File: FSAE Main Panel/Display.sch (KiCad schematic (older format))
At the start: 7 parts

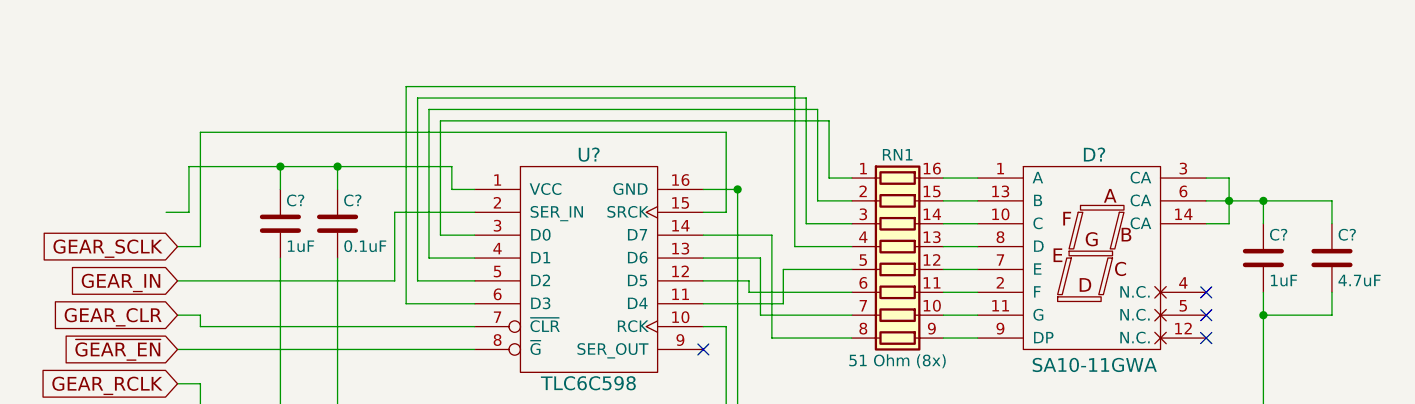
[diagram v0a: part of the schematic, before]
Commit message: Attempt to fix custom library pathing
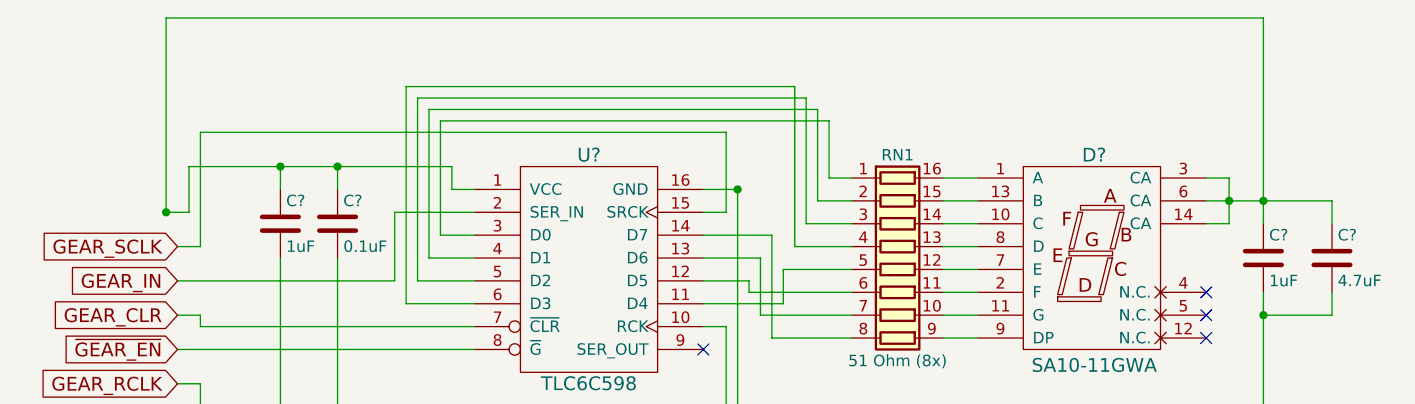
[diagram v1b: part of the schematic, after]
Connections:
- net at C?.1, C?.1, U?.1 (VCC): now also C?.1, C?.1, D?.14 (CA), D?.3 (CA), D?.6 (CA)
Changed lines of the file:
@@
 LIBS:contrib
 LIBS:valves
-LIBS:KingBright_Addition
-LIBS:TI_Additions
+LIBS:apa102c
+LIBS:lm2734
+LIBS:prtr5v0u2x
+LIBS:samd21g18a-au
 LIBS:FSAE Main Panel-cache
 EELAYER 25 0
@@
 $EndComp
 Wire Wire Line
-	6150 4900 6150 5000
+	6150 4100 6150 5000
 Wire Wire Line
 	6450 4900 6450 5000
@@
 	2100 5150 2100 5950
 Connection ~ 2100 5950
+Wire Wire Line
+	6150 4100 1350 4100
+Wire Wire Line
+	1350 4100 1350 4950
+Connection ~ 1350 4950
 $EndSCHEMATC

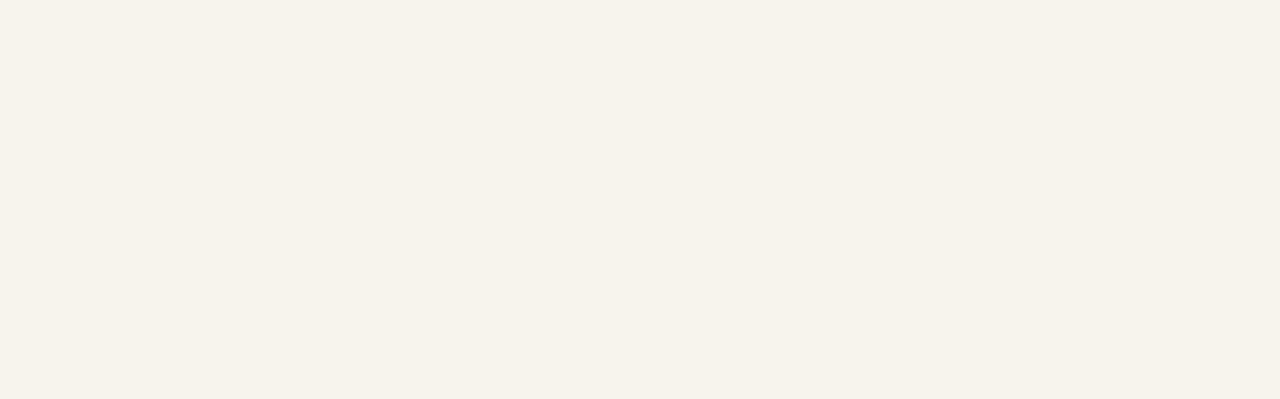
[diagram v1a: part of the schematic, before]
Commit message: Initial PCB layout
Started PCB layout with major dimensions.
Added RPM LEDs.
Rearranged the file structure for the librarys and the search paths.
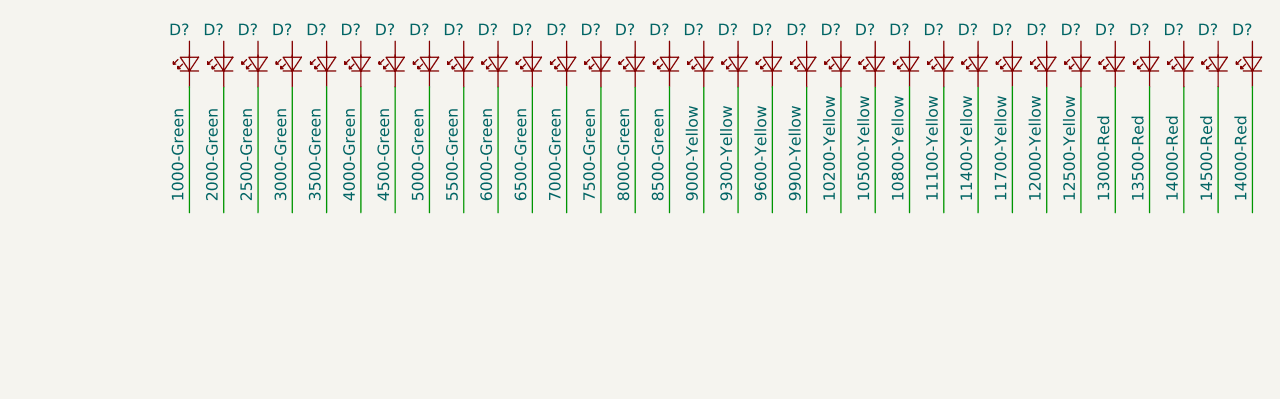
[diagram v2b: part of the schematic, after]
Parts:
- added D?: 2000-Green, OSRAM:D_0805, symbol LED_Small
- added D?: 1000-Green, OSRAM:D_0805, symbol LED_Small
- added D?: 2500-Green, OSRAM:D_0805, symbol LED_Small
- added D?: 3500-Green, OSRAM:D_0805, symbol LED_Small
- added D?: 3000-Green, OSRAM:D_0805, symbol LED_Small
- added D?: 4000-Green, OSRAM:D_0805, symbol LED_Small
- added D?: 5000-Green, OSRAM:D_0805, symbol LED_Small
- added D?: 4500-Green, OSRAM:D_0805, symbol LED_Small
- added D?: 5500-Green, OSRAM:D_0805, symbol LED_Small
- added D?: 6500-Green, OSRAM:D_0805, symbol LED_Small
- added D?: 6000-Green, OSRAM:D_0805, symbol LED_Small
- added D?: 7000-Green, OSRAM:D_0805, symbol LED_Small
- added D?: 8000-Green, OSRAM:D_0805, symbol LED_Small
- added D?: 7500-Green, OSRAM:D_0805, symbol LED_Small
- added D?: 8500-Green, OSRAM:D_0805, symbol LED_Small
- added D?: 9300-Yellow, OSRAM:D_0805, symbol LED_Small
- added D?: 9000-Yellow, OSRAM:D_0805, symbol LED_Small
- added D?: 9600-Yellow, OSRAM:D_0805, symbol LED_Small
- added D?: 10200-Yellow, OSRAM:D_0805, symbol LED_Small
- added D?: 9900-Yellow, OSRAM:D_0805, symbol LED_Small
- added D?: 10500-Yellow, OSRAM:D_0805, symbol LED_Small
- added D?: 11100-Yellow, OSRAM:D_0805, symbol LED_Small
- added D?: 10800-Yellow, OSRAM:D_0805, symbol LED_Small
- added D?: 11400-Yellow, OSRAM:D_0805, symbol LED_Small
- added D?: 11700-Yellow, OSRAM:D_0805, symbol LED_Small
- added D?: 12000-Yellow, OSRAM:D_0805, symbol LED_Small
- added D?: 13000-Red, OSRAM:D_0805, symbol LED_Small
- added D?: 12500-Yellow, OSRAM:D_0805, symbol LED_Small
- added D?: 13500-Red, OSRAM:D_0805, symbol LED_Small
- added D?: 14500-Red, OSRAM:D_0805, symbol LED_Small
- added D? (x2): 14000-Red, OSRAM:D_0805, symbol LED_Small
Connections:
- wire segments 80 -> 112

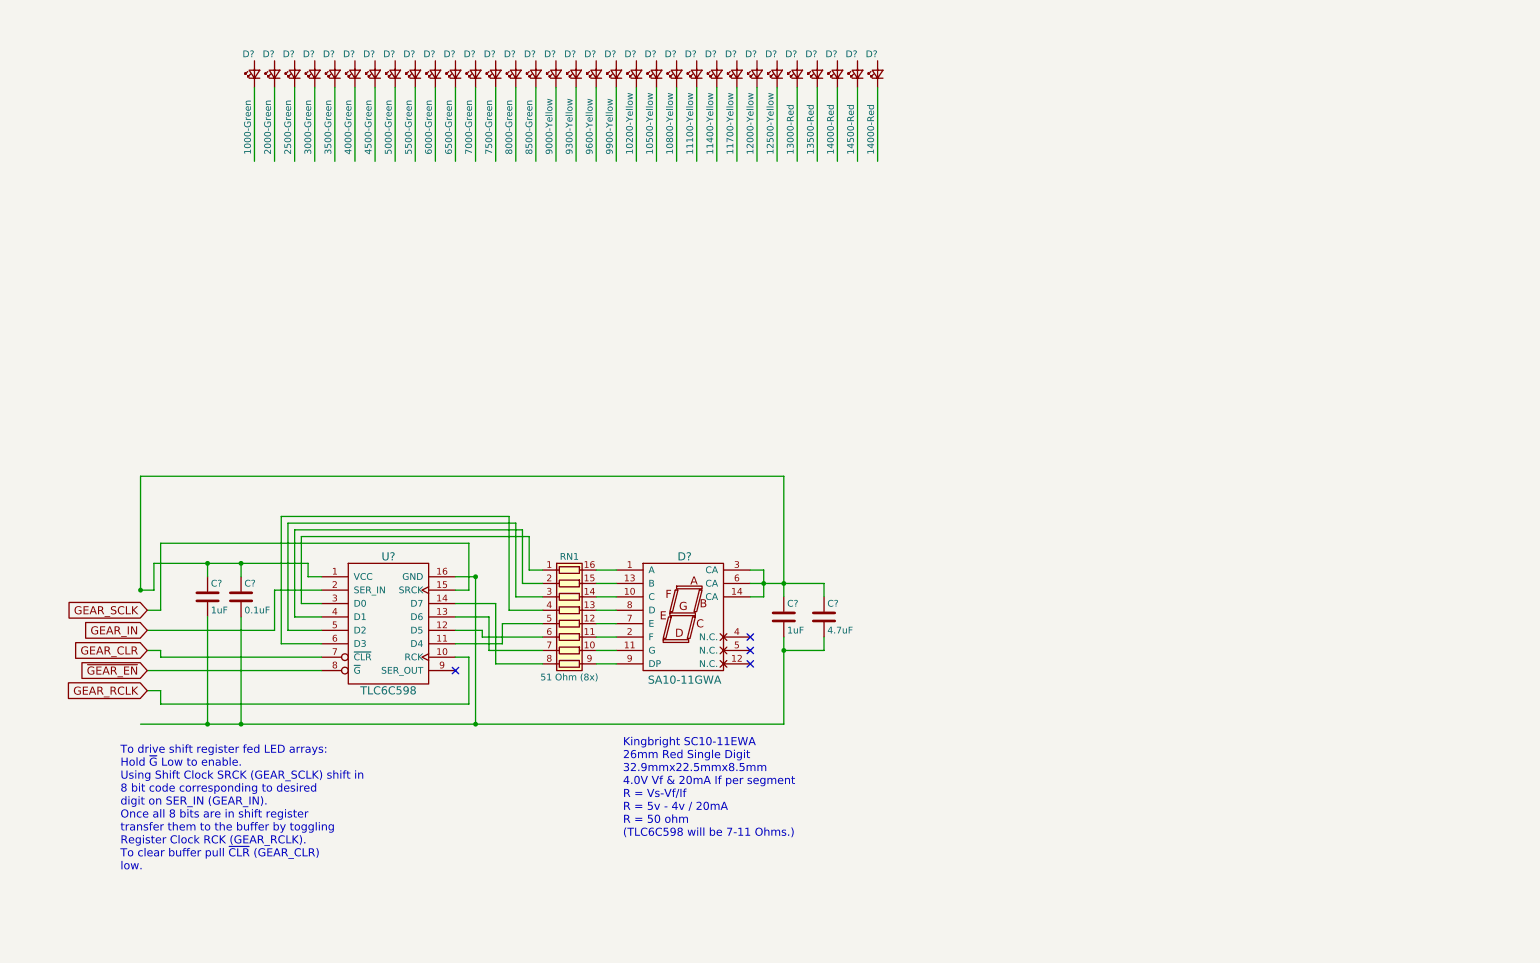
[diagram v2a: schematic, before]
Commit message: Added RPM LED Control
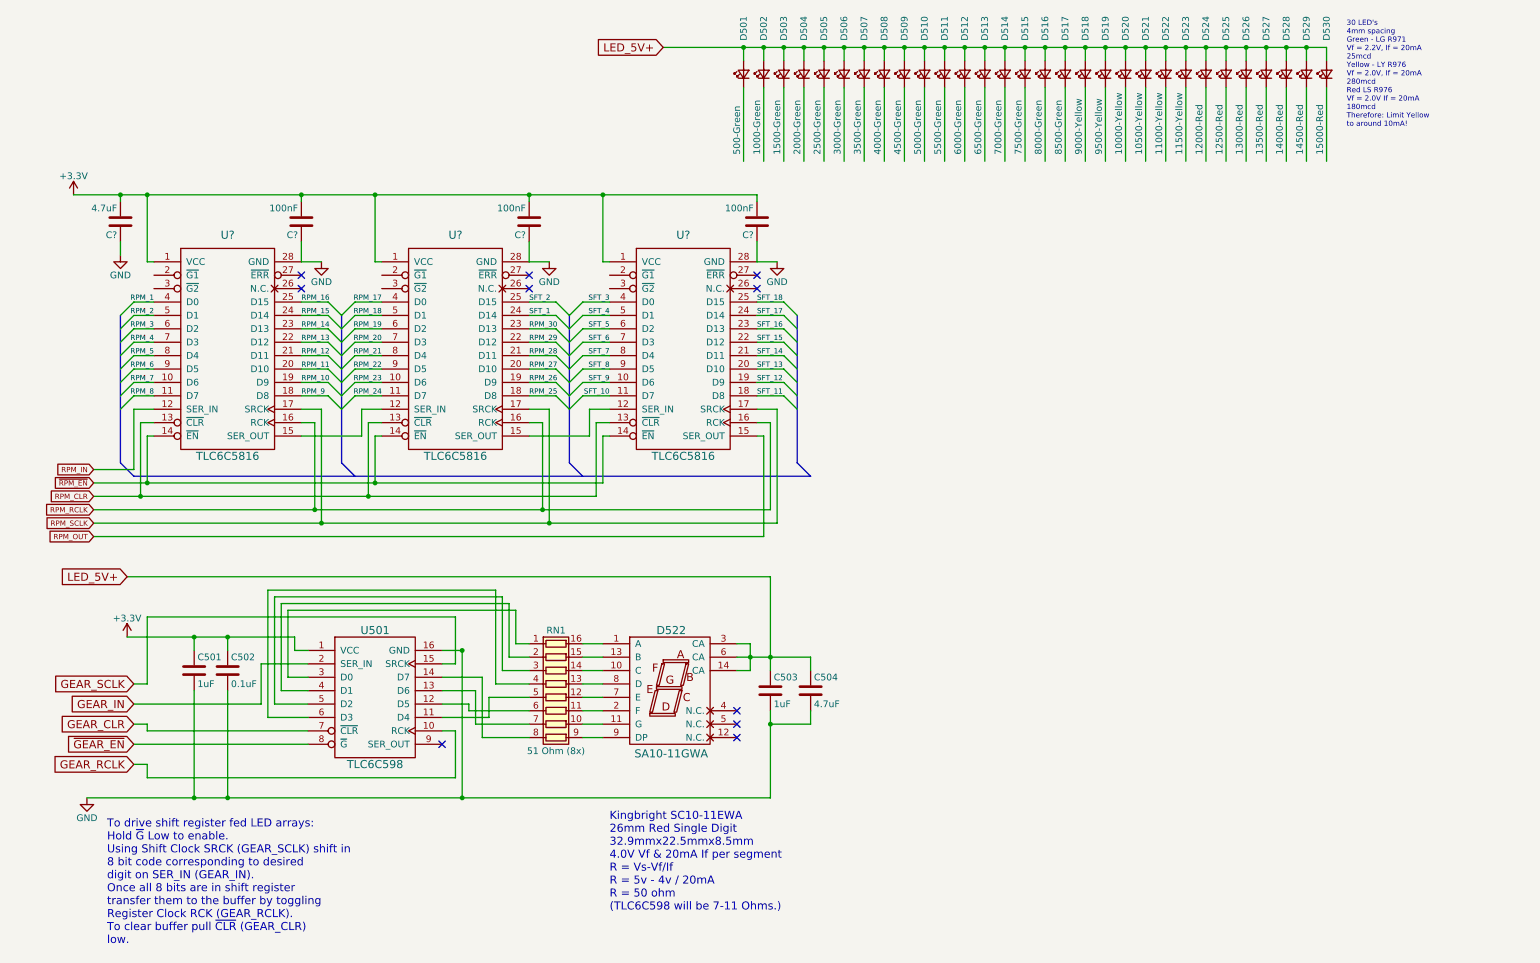
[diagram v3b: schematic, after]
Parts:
- removed D?: 11400-Yellow, OSRAM:D_0805, symbol LED_Small
- removed D?: 11700-Yellow, OSRAM:D_0805, symbol LED_Small
- removed D?: 12000-Yellow, OSRAM:D_0805, symbol LED_Small
- removed D?: 12500-Yellow, OSRAM:D_0805, symbol LED_Small
- added C? (x3): 100nF, symbol C
- added C?: 4.7uF, symbol C
- added D529: 14500-Red, LEDs:LED_0805, symbol LED_Small
- added D530: 15000-Red, LEDs:LED_0805, symbol LED_Small
- added U? (x3): TLC6C5816, symbol TLC6C5816
- D501: renamed from D?; value 1000-Green -> 500-Green; footprint OSRAM:D_0805 -> LEDs:LED_0805
- D502: renamed from D?; value 2000-Green -> 1000-Green; footprint OSRAM:D_0805 -> LEDs:LED_0805
- D503: renamed from D?; value 2500-Green -> 1500-Green; footprint OSRAM:D_0805 -> LEDs:LED_0805
- D504: renamed from D?; value 3000-Green -> 2000-Green; footprint OSRAM:D_0805 -> LEDs:LED_0805
- D505: renamed from D?; value 3500-Green -> 2500-Green; footprint OSRAM:D_0805 -> LEDs:LED_0805
- D506: renamed from D?; value 4000-Green -> 3000-Green; footprint OSRAM:D_0805 -> LEDs:LED_0805
- D507: renamed from D?; value 4500-Green -> 3500-Green; footprint OSRAM:D_0805 -> LEDs:LED_0805
- D508: renamed from D?; value 5000-Green -> 4000-Green; footprint OSRAM:D_0805 -> LEDs:LED_0805
- D509: renamed from D?; value 5500-Green -> 4500-Green; footprint OSRAM:D_0805 -> LEDs:LED_0805
- D510: renamed from D?; value 6000-Green -> 5000-Green; footprint OSRAM:D_0805 -> LEDs:LED_0805
- D511: renamed from D?; value 6500-Green -> 5500-Green; footprint OSRAM:D_0805 -> LEDs:LED_0805
- D512: renamed from D?; value 7000-Green -> 6000-Green; footprint OSRAM:D_0805 -> LEDs:LED_0805
- D513: renamed from D?; value 7500-Green -> 6500-Green; footprint OSRAM:D_0805 -> LEDs:LED_0805
- D514: renamed from D?; value 8000-Green -> 7000-Green; footprint OSRAM:D_0805 -> LEDs:LED_0805
- D515: renamed from D?; value 8500-Green -> 7500-Green; footprint OSRAM:D_0805 -> LEDs:LED_0805
- D516: renamed from D?; value 9000-Yellow -> 8000-Green; footprint OSRAM:D_0805 -> LEDs:LED_0805
- D517: renamed from D?; value 9300-Yellow -> 8500-Green; footprint OSRAM:D_0805 -> LEDs:LED_0805
- D518: renamed from D?; value 9600-Yellow -> 9000-Yellow; footprint OSRAM:D_0805 -> LEDs:LED_0805; Part Number LG R971 -> LY R976
- D519: renamed from D?; value 9900-Yellow -> 9500-Yellow; footprint OSRAM:D_0805 -> LEDs:LED_0805; Part Number LG R971 -> LY R976
- D520: renamed from D?; value 10200-Yellow -> 10000-Yellow; footprint OSRAM:D_0805 -> LEDs:LED_0805; Part Number LG R971 -> LY R976
- D521: renamed from D?; footprint OSRAM:D_0805 -> LEDs:LED_0805; Part Number LG R971 -> LY R976
- D522: renamed from D?; footprint (none) -> Kingbright:SC10-11EWA
- D522: renamed from D?; value 10800-Yellow -> 11000-Yellow; footprint OSRAM:D_0805 -> LEDs:LED_0805; Part Number LG R971 -> LY R976
- D523: renamed from D?; value 11100-Yellow -> 11500-Yellow; footprint OSRAM:D_0805 -> LEDs:LED_0805; Part Number LG R971 -> LY R976
- D524: renamed from D?; value 13000-Red -> 12000-Red; footprint OSRAM:D_0805 -> LEDs:LED_0805
- D525: renamed from D?; value 13500-Red -> 12500-Red; footprint OSRAM:D_0805 -> LEDs:LED_0805
- D526: renamed from D?; value 14000-Red -> 13000-Red; footprint OSRAM:D_0805 -> LEDs:LED_0805
- D527: renamed from D?; value 14500-Red -> 13500-Red; footprint OSRAM:D_0805 -> LEDs:LED_0805
- D528: renamed from D?; footprint OSRAM:D_0805 -> LEDs:LED_0805
- gave numbers to parts that had none: 5
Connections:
- net labels added: +3.3V, GND, LED_5V+, RPM_1, RPM_10, RPM_11, RPM_12, RPM_13, RPM_14, RPM_15, RPM_16, RPM_17, RPM_18, RPM_19, RPM_2, RPM_20, RPM_21, RPM_22, RPM_23, RPM_24, RPM_25, RPM_26, RPM_27, RPM_28, RPM_29, RPM_3, RPM_30, RPM_4, RPM_5, RPM_6, RPM_7, RPM_8, RPM_9, RPM_CLR, RPM_IN, RPM_OUT, RPM_RCLK, RPM_SCLK, SFT_1, SFT_10, SFT_11, SFT_12, SFT_13, SFT_14, SFT_15, SFT_16, SFT_17, SFT_18, SFT_2, SFT_3, SFT_4, SFT_5, SFT_6, SFT_7, SFT_8, SFT_9, ~RPM_EN
- wire segments 112 -> 244
- no-connect marks 4 -> 10
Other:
- note added: "30 LED's\n4mm spacing\nGreen - LG R971\nVf = 2.2V, If = 20mA\n25mcd\nYellow - LY R976\nVf = 2.0V, If = 20mA\n280mcd\nRed LS R976\nVf = 2.0V If = 20mA\n180mcd\nTherefore: Limit Yellow\nto around 10mA!"
- moved on the sheet: C501, C502, C503, C504, D501, D502, D503, D504, D505, D506, D507, D508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
